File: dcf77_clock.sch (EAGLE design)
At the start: 42 parts, among them IC1 DS1307SO8, IC2 7805DT, IC3 ATMEGA48/88/168-AU, J1 DCJ0202, Q1 32.768kHz, Q2 IRLML6244TRPBF, SW1 EC12E_SW, U1 AVR_SPI_PROG2PTH2, U2 LCD-16X2UPPERHOLES

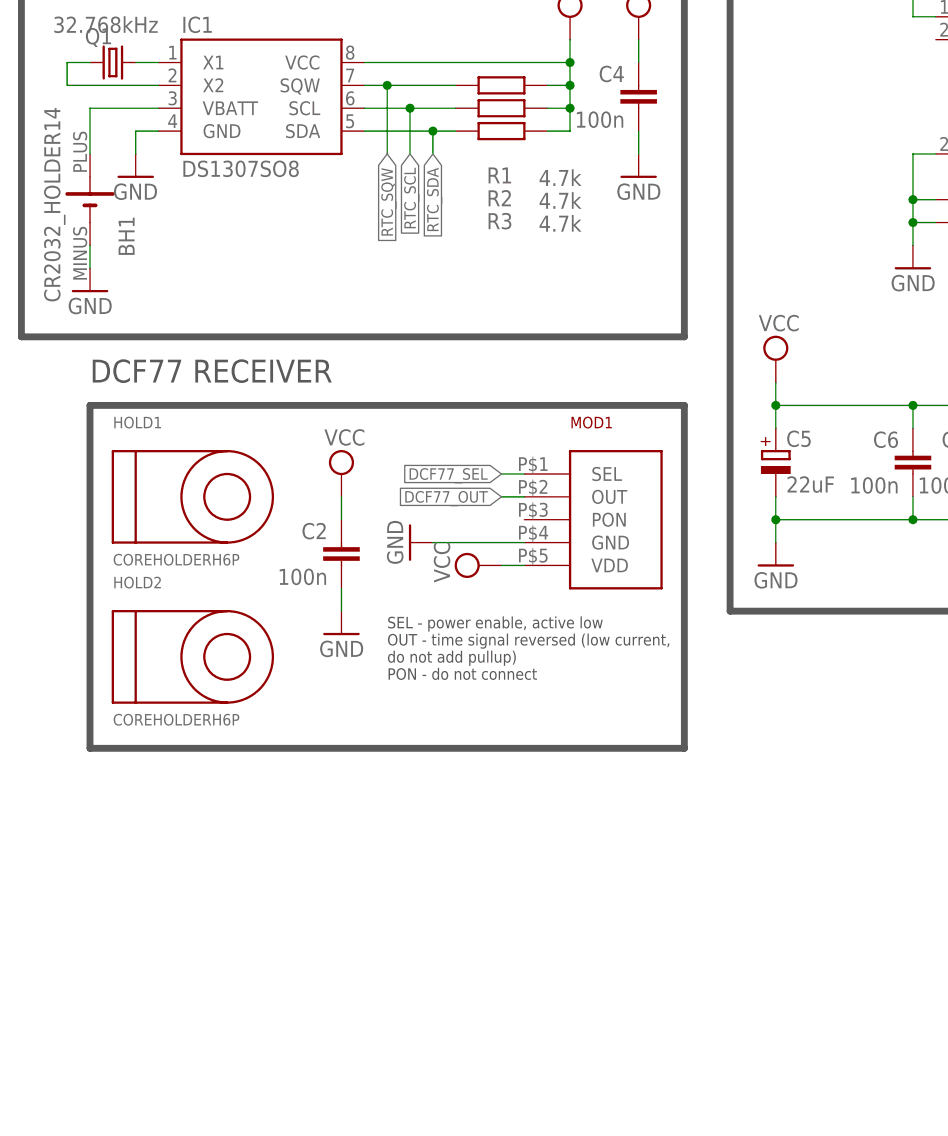
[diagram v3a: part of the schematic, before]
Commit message: Add 3V3 LDO and level shifter for MAS6181B
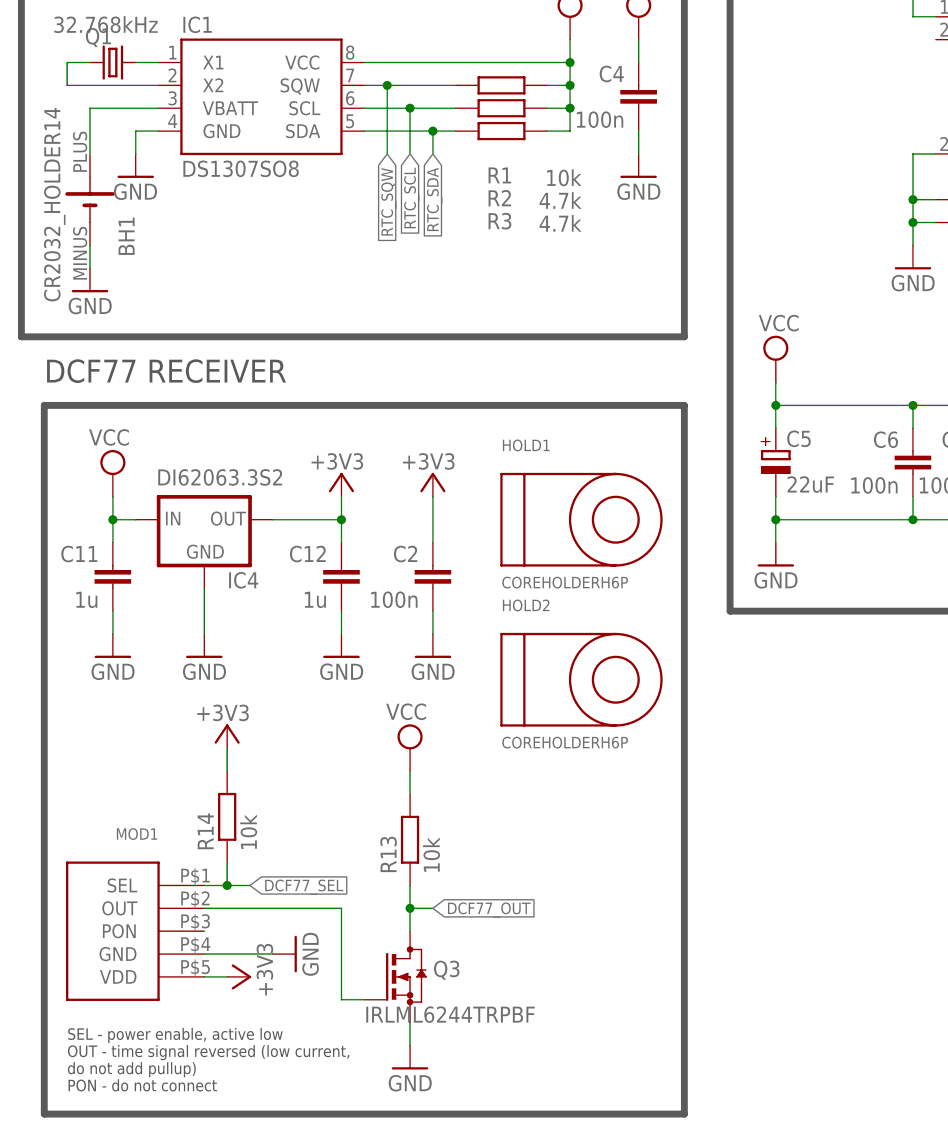
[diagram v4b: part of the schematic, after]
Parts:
- added C11, C12: 1u, rcl:C-EUC0805K
- added IC4: DI62063.3S2, dcf77:DI62063.3S2
- added Q3: IRLML6244TRPBF, sosbutton:IRLML6244TRPBF
- added R13, R14: 10k, rcl:R-EU_M0805
- R1: value 4.7k -> 10k
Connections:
- new net +3V3: C12.1, C2.1, IC4.OUT, MOD1.VDD, R14.2
- new net N$6: MOD1.OUT, Q3.G
- net DCF77_OUT: now also Q3.D, R13.1; no longer MOD1.OUT
- net DCF77_SEL: now also R14.1
- net GND: now also C11.2, C12.2, IC4.GND, Q3.S
- net VCC: now also C11.1, IC4.IN, R13.2; no longer C2.1, MOD1.VDD
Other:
- moved on the sheet: C2, HOLD1, HOLD2, MOD1

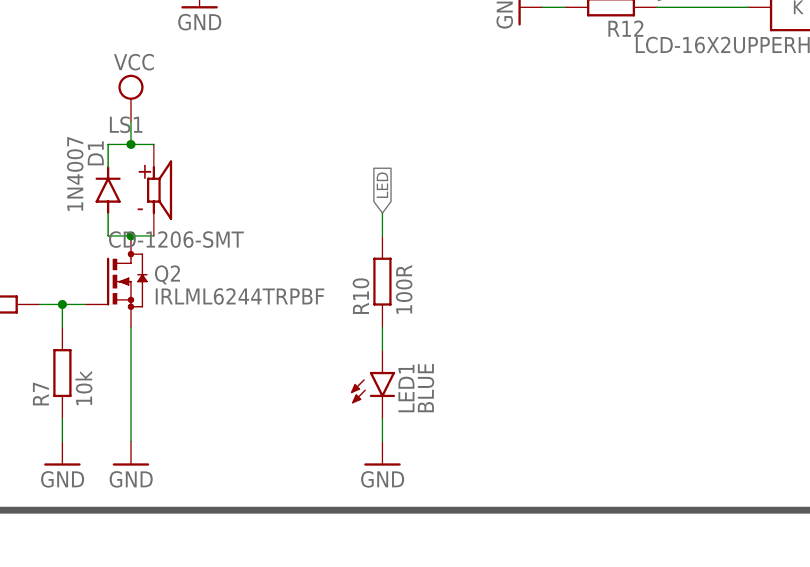
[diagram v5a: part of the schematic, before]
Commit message: Change LED resistor to limit brightness
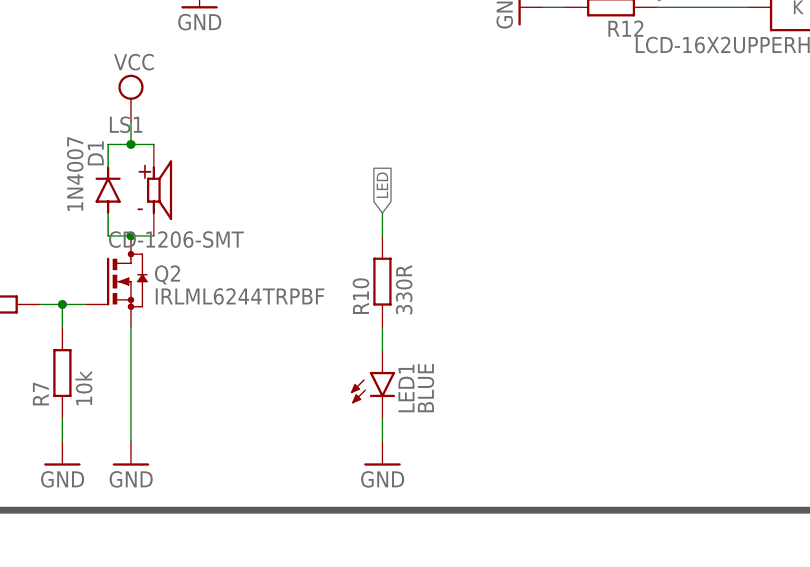
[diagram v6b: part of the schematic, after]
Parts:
- R10: value 100R -> 330R
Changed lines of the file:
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@@
 <part name="GND9" library="supply1" library_urn="urn:adsk.eagle:library:371" deviceset="GND" device=""/>
 <part name="GND10" library="supply1" library_urn="urn:adsk.eagle:library:371" deviceset="GND" device=""/>
-<part name="R10" library="rcl" library_urn="urn:adsk.eagle:library:334" deviceset="R-EU_" device="M0805" package3d_urn="urn:adsk.eagle:package:23556/2" value="100R"/>
+<part name="R10" library="rcl" library_urn="urn:adsk.eagle:library:334" deviceset="R-EU_" device="M0805" package3d_urn="urn:adsk.eagle:package:23556/2" value="330R"/>
 <part name="GND12" library="supply1" library_urn="urn:adsk.eagle:library:371" deviceset="GND" device=""/>
 <part name="R5" library="rcl" library_urn="urn:adsk.eagle:library:334" deviceset="R-EU_" device="M0805" package3d_urn="urn:adsk.eagle:package:23556/2" value="10k"/>
